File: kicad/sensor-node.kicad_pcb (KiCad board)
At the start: 2 copper layers, 22 parts

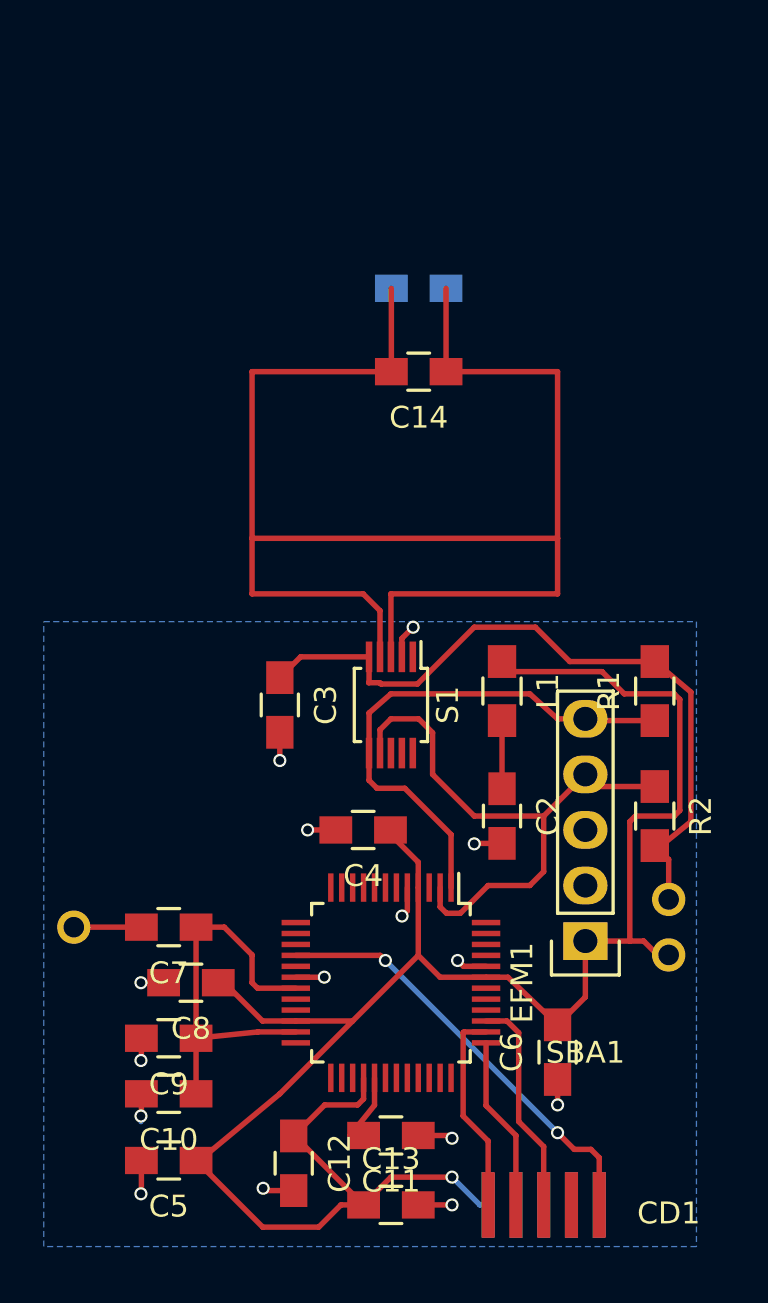
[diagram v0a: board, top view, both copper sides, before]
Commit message: minor routing changes
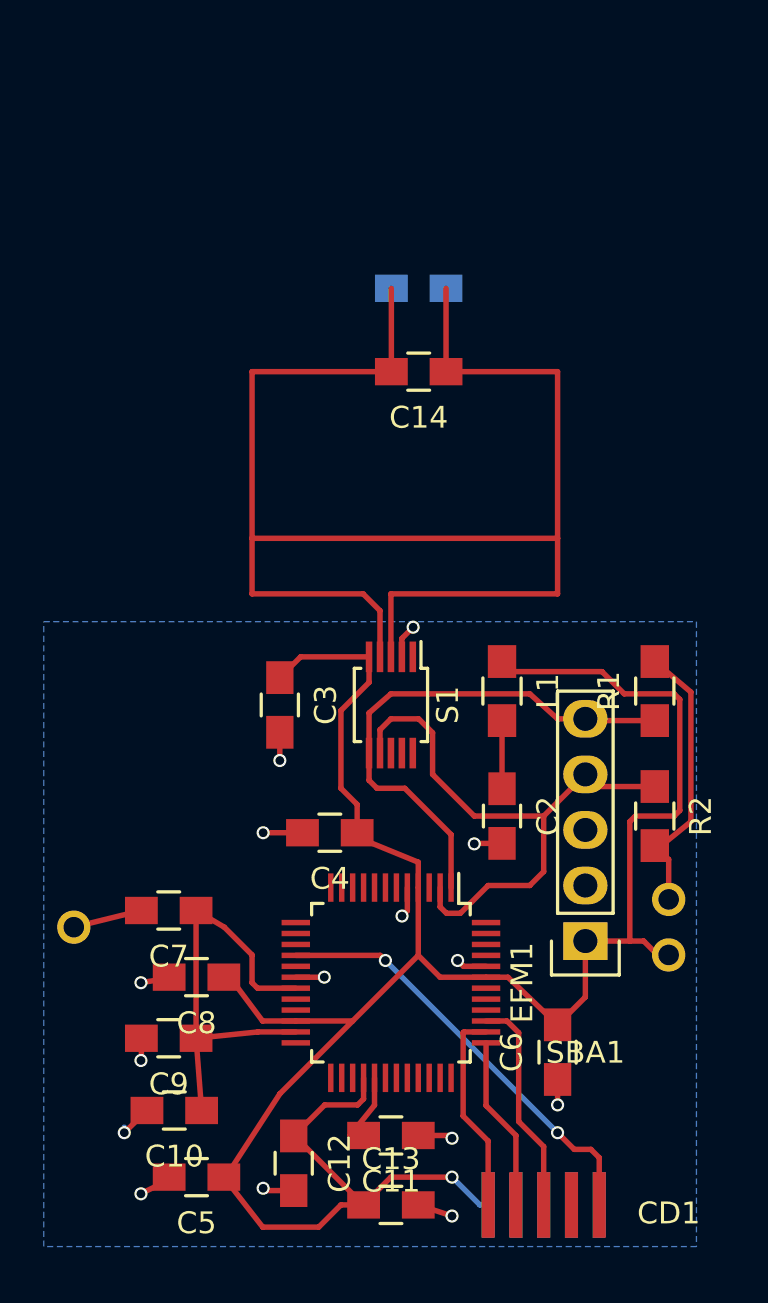
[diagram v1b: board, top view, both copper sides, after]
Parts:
- moved C4 1.53 mm to (149.6, 93.5)
- moved C5 1.48 mm to (143.5, 109.2)
- moved C10 0.80 mm to (142.5, 106.2)
- moved C7 0.76 mm to (142.2, 97.0)
- moved C8 0.36 mm to (143.5, 100.1)
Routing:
- net +3V3: track 142.6 -> 136.8 mm
- net GND: track 23.4 -> 24.8 mm

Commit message: improved routing
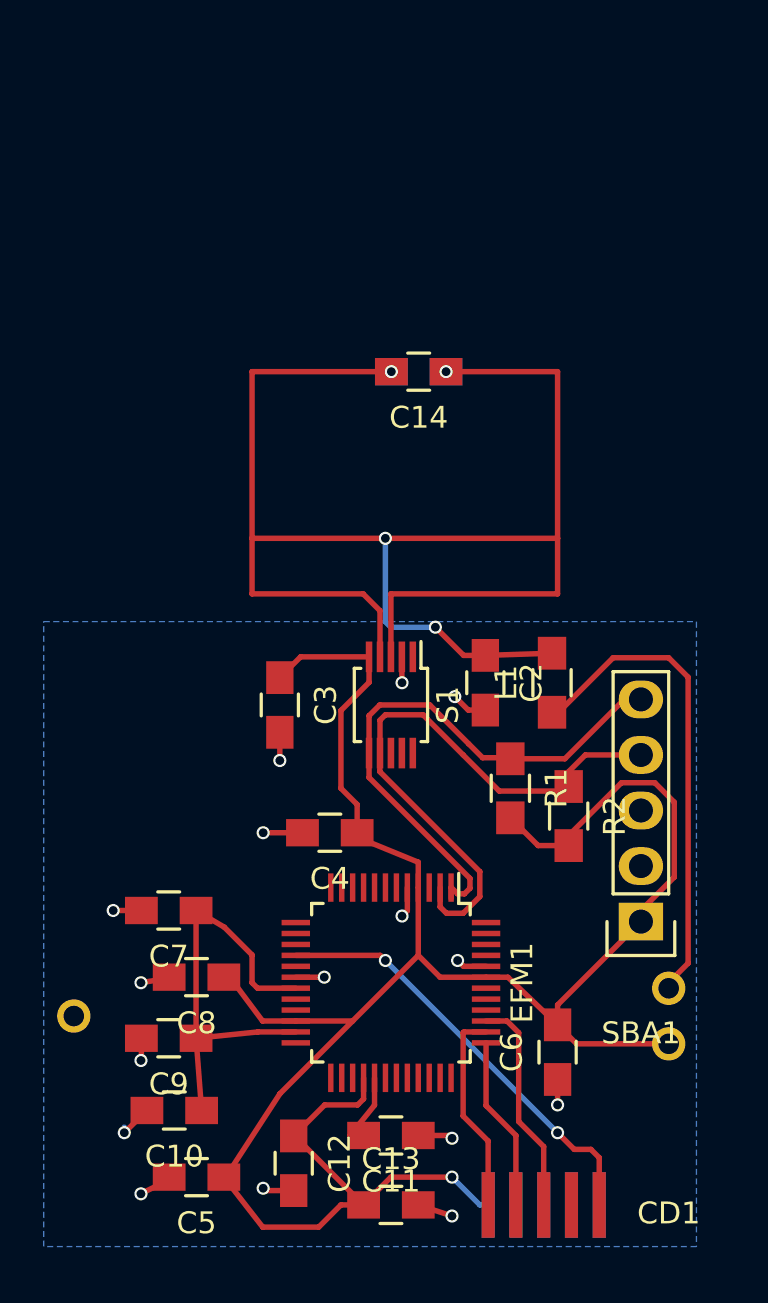
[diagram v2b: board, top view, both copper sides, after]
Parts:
- moved R1 7.96 mm to (157.9, 91.4), turned to 270 degrees
- moved C2 6.14 mm to (156.7, 86.6)
- moved BT1 4.06 mm to (165.1, 101.9)
- moved R2 3.94 mm to (160.5, 92.7)
- moved C1 3.81 mm to (153.7, 72.4)
- moved SBA1 2.69 mm to (163.8, 97.5)
- moved L1 2.32 mm to (159.8, 86.6), turned to 90 degrees
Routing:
- net +3V3: track 136.8 -> 145.0 mm
- net /SDA: track 24.1 -> 26.3 mm
- net /SCL: track 26.9 -> 28.9 mm
- net GND: track 24.8 -> 22.9 mm, vias 15 -> 16
- net Net-(C1-Pad1): track 75.3 -> 76.6 mm, vias 0 -> 4

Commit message: more routing
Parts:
- moved C13 4.96 mm to (147.4, 110.2), turned to 180 degrees
- moved CD1 3.32 mm to (153.5, 110.9)
- moved C7 1.94 mm to (144.2, 97.3)
- moved C11 1.73 mm to (151.4, 108.7), turned to 90 degrees
- moved C5 1.63 mm to (141.9, 109.2)
- moved C12 1.33 mm to (147.6, 107.3), turned to 180 degrees
- moved C3 1.14 mm to (148.5, 87.6)
- moved C10 1.02 mm to (141.6, 105.7)
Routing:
- net /~RESET: track 19.9 -> 17.3 mm
- net /SDA: track 26.3 -> 27.8 mm
- net /SCL: track 28.9 -> 27.7 mm
- net +3V3: track 145.0 -> 144.2 mm
- net Net-(C11-Pad2): track 3.69 -> 2.89 mm
- net /SWDIO: track 9.41 -> 10.1 mm
- net GND: track 22.9 -> 22.8 mm, vias 16 -> 15

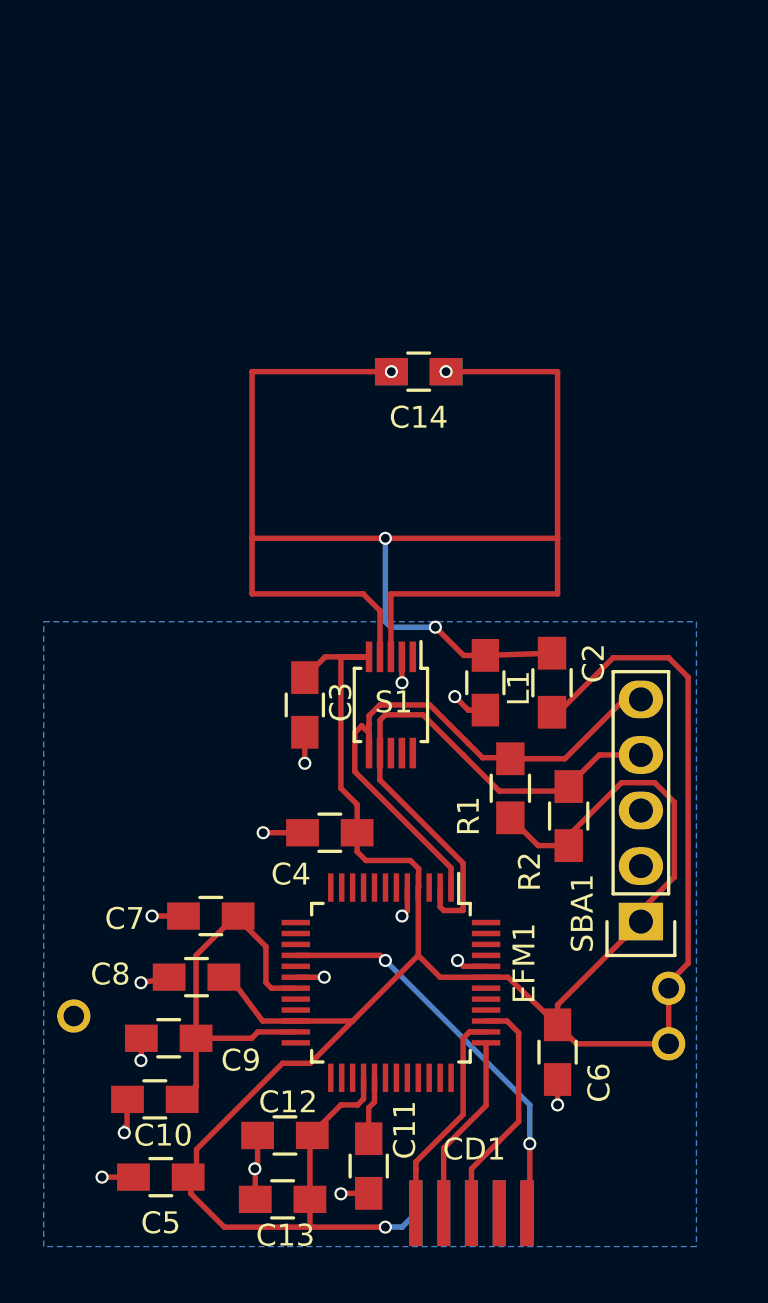
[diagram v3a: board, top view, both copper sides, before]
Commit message: added mounting holes and custom footprint for sensor module
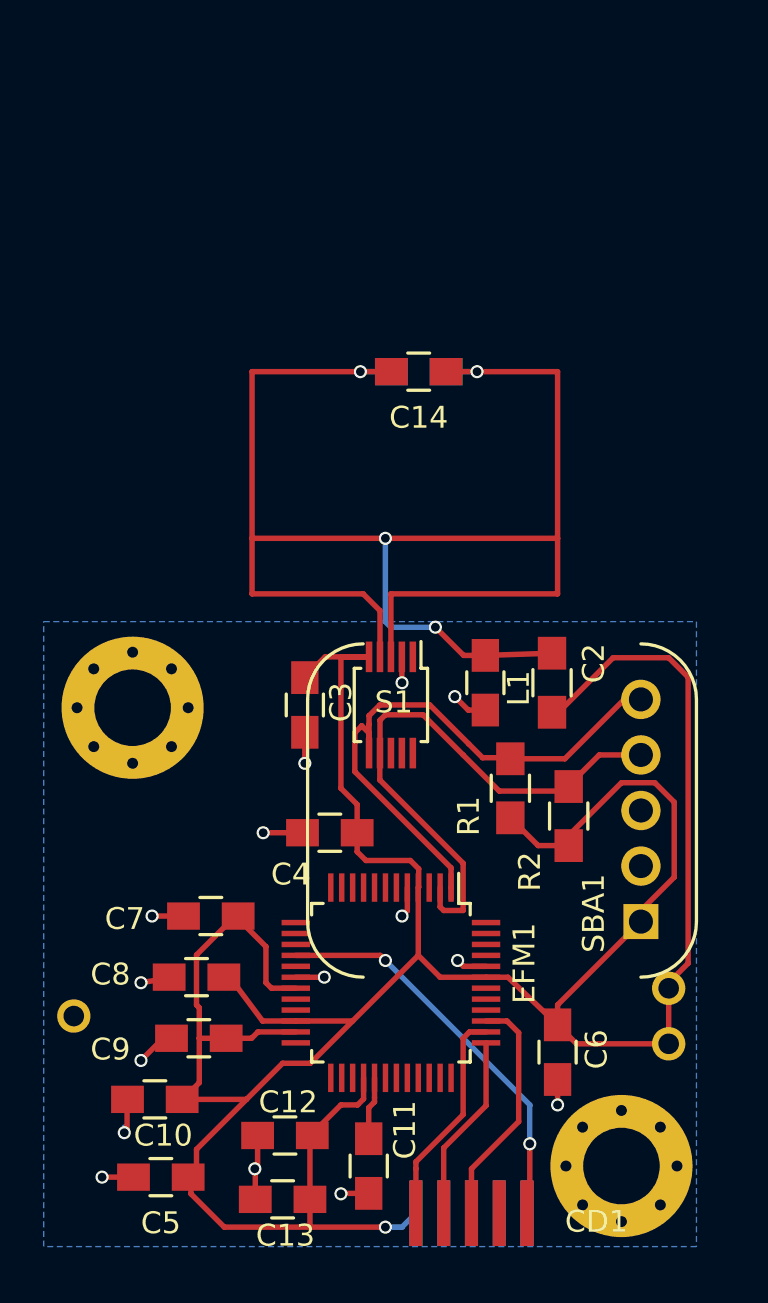
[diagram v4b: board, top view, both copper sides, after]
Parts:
- added REF**: mounting, sensor-node:mounting, F.Cu at (140.6, 87.8)
- added REF**: mounting, sensor-node:mounting, F.Cu at (162.9, 108.7)
- BT1: footprint HU2032-LF -> sensor-node:HU2032-LF
- CD1: footprint CORTEX-DEBUG-EDGE -> sensor-node:CORTEX-DEBUG-EDGE
- SBA1: footprint Pin_Headers:Pin_Header_Straight_1x05 -> sensor-node:Si7021BA
- moved SBA1 5.08 mm to (163.8, 92.5), turned to 90 degrees
- moved C9 1.38 mm to (143.6, 102.9)
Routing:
- net +3V3: track 144.2 -> 147.1 mm
- net Net-(C1-Pad1): track 76.6 -> 79.4 mm
- net GND: track 22.8 -> 23.6 mm

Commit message: added board outline
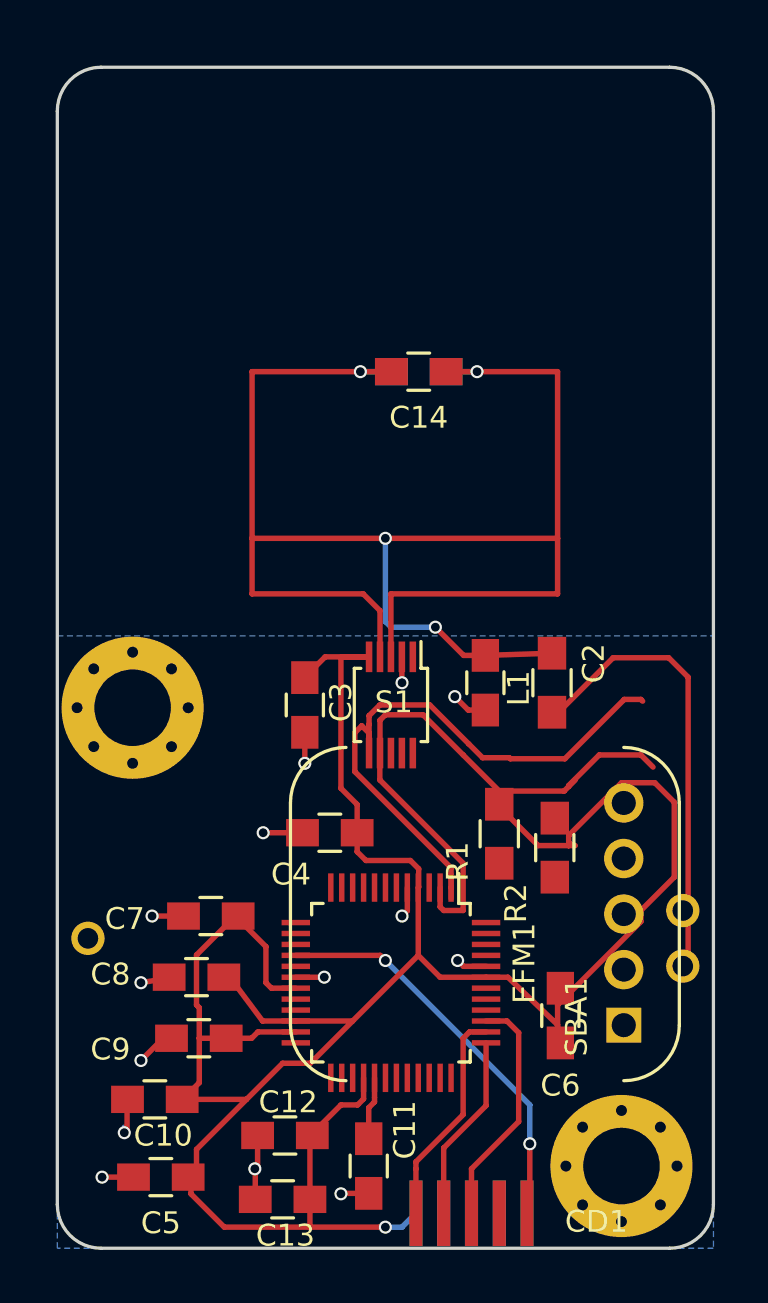
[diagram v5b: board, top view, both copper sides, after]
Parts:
- moved SBA1 4.80 mm to (163.0, 97.2)
- moved BT1 3.61 mm to (165.7, 98.3)
- moved R1 2.14 mm to (157.4, 93.5)
- moved C6 1.68 mm to (160.1, 101.8), turned to 270 degrees
- moved R2 1.58 mm to (159.9, 94.2)
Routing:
- net +3V3: track 147.1 -> 121.1 mm
- net /SDA: track 27.8 -> 52.3 mm
- net /SCL: track 27.7 -> 14.4 mm
- net (no net): track 0.00 -> 4.71 mm
- net GND: track 23.6 -> 22.5 mm, vias 15 -> 14
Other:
- board outline added: 30 x 54 mm

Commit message: more rounting and antenna planning
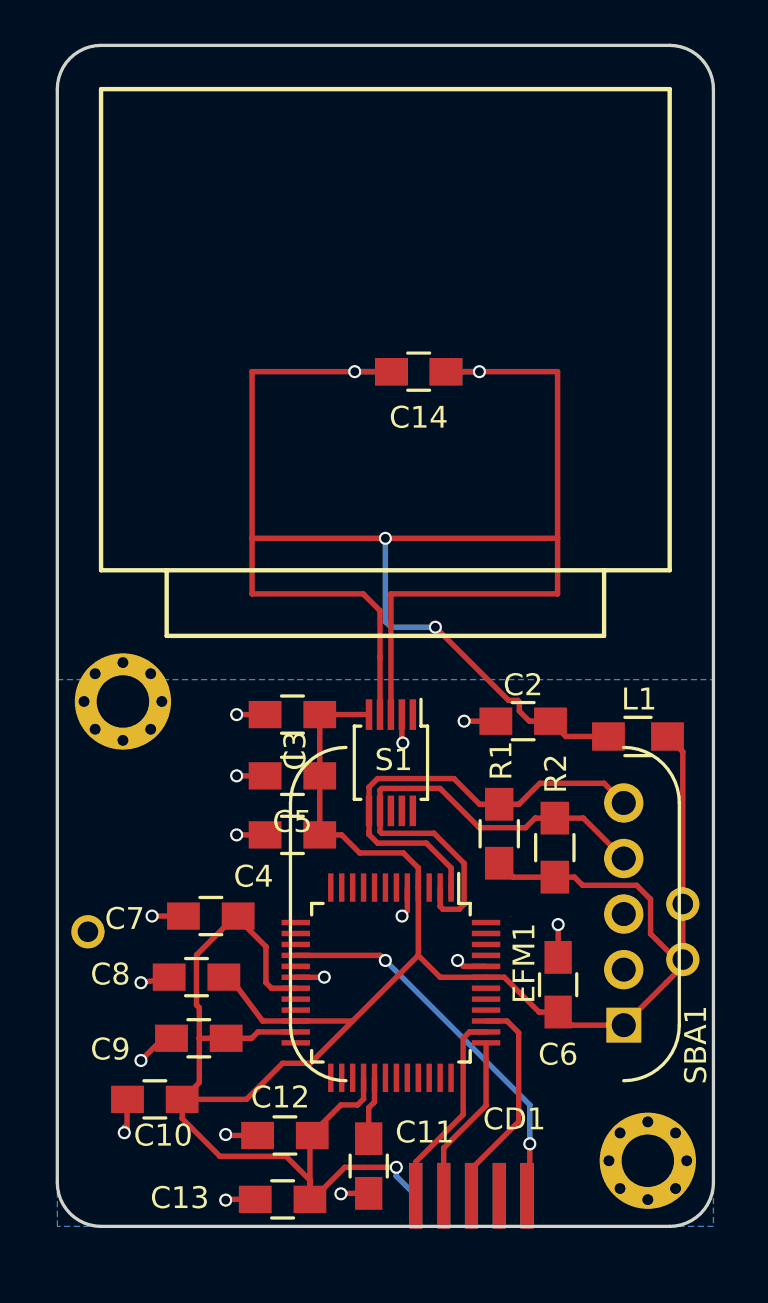
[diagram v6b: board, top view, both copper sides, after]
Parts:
- removed the REF** at (140.6, 87.8)
- removed the REF** at (162.9, 108.7)
- added REF**: mounting, sensor-node:mounting, F.Cu at (140.1, 87.5)
- added REF**: mounting, sensor-node:mounting, F.Cu at (164.1, 108.5)
- moved C5 19.3 mm to (147.9, 90.9)
- moved L1 4.63 mm to (163.7, 89.1), turned to 180 degrees
- moved S1 2.64 mm to (152.4, 90.3)
- moved C2 2.46 mm to (158.4, 88.4), turned to 180 degrees
- moved C4 1.71 mm to (147.9, 93.6)
- moved C6 1.42 mm to (160.0, 100.4)
- moved CD1 0.80 mm to (153.5, 110.1)
- moved C3 0.72 mm to (147.9, 88.1), turned to 180 degrees
- moved BT1 0.30 mm to (165.7, 98.0)
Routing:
- net /SDA: track 52.3 -> 21.0 mm
- net Net-(C1-Pad1): track 79.4 -> 89.5 mm
- net /SCL: track 14.4 -> 23.2 mm
- net +3V3: track 121.1 -> 115.1 mm
- net (no net): track 4.71 -> 0.00 mm
- net GND: track 22.5 -> 23.0 mm, vias 14 -> 16

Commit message: redrew antenna
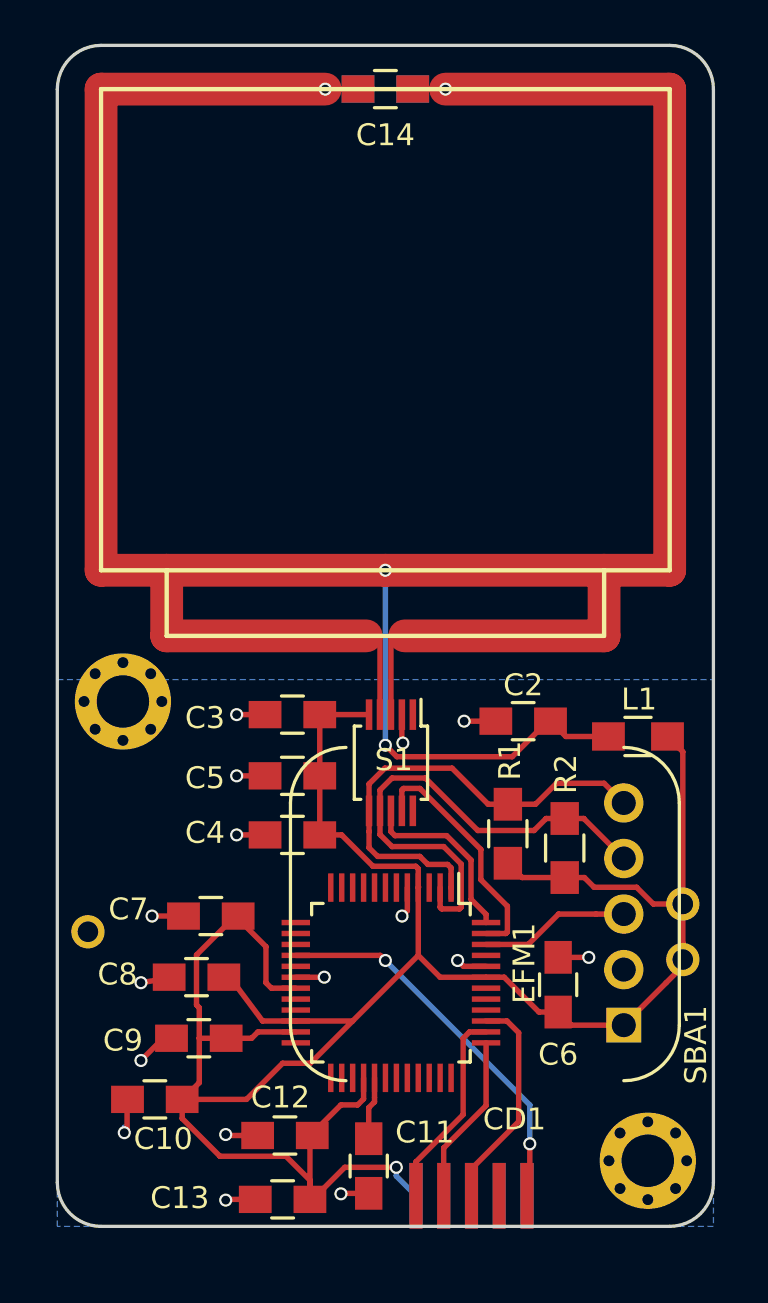
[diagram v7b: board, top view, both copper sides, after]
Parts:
- moved C1 13.0 mm to (152.1, 59.5)
- moved C14 13.0 mm to (152.1, 59.5)
- moved R2 0.45 mm to (160.3, 94.2)
- moved R1 0.39 mm to (157.7, 93.5)
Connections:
- EFM1 pad 46: (no net) -> /~SEN_ENABLE
- EFM1 pad 47: (no net) -> /RAD_INT
- EFM1 pad 48: (no net) -> /RAD_ENABLE
- S1 pad 8: (no net) -> /RAD_ENABLE
- S1 pad 9: (no net) -> /RAD_INT
- SBA1 pad 3: (no net) -> /~SEN_ENABLE
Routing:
- net Net-(C1-Pad1): track 89.5 -> 148.6 mm
- net /RAD_INT: track 0.00 -> 11.0 mm
- net /RAD_ENABLE: track 0.00 -> 8.30 mm
- net /~SEN_ENABLE: track 0.00 -> 6.87 mm
- net /SDA: track 21.0 -> 22.8 mm
- net +3V3: track 115.1 -> 113.5 mm
